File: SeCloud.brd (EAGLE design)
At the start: 107.2 x 69.7 mm, 94 parts, among them Q1 E4SB25.000F20E15(25MHz/20pF/2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, U3 SY6280, U7 MP1482DS, U8 RTL8211CL-GR

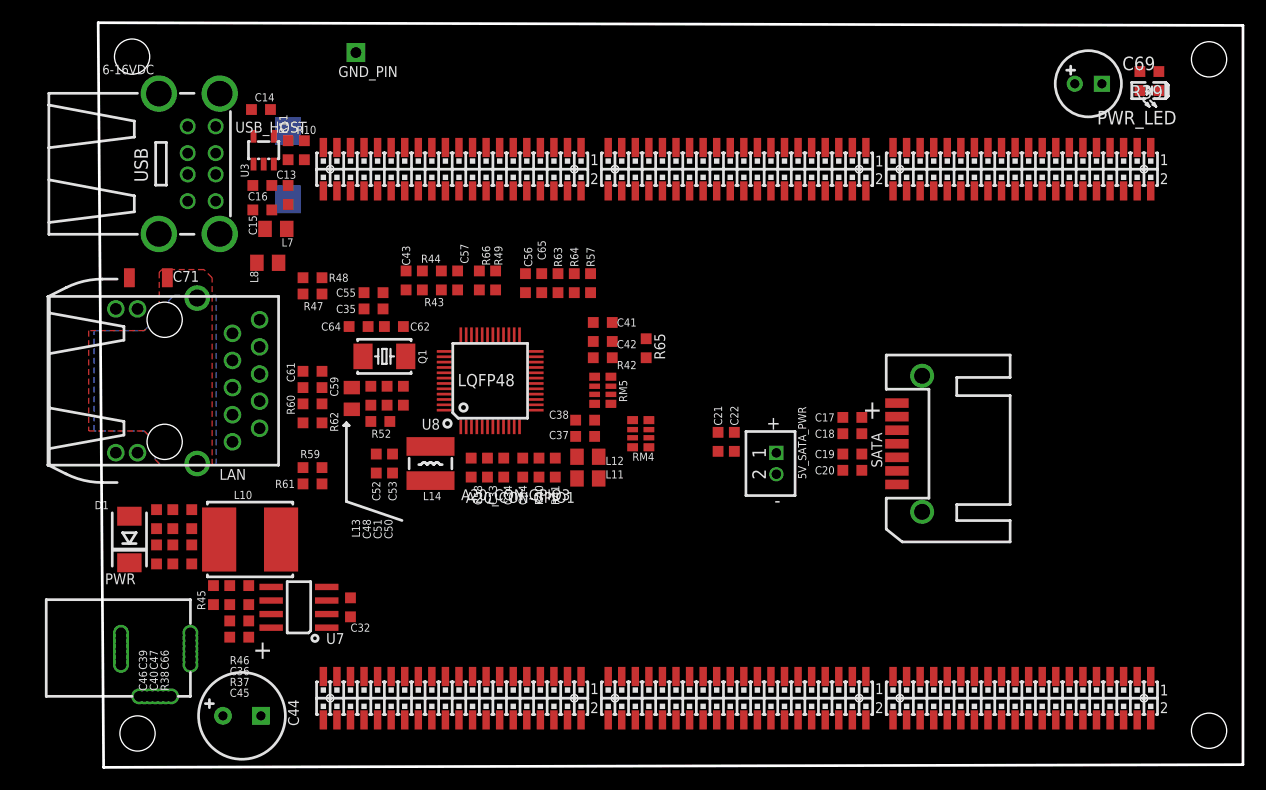
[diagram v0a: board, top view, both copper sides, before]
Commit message: Added lbr, RTL8188 module, and SATA connector;
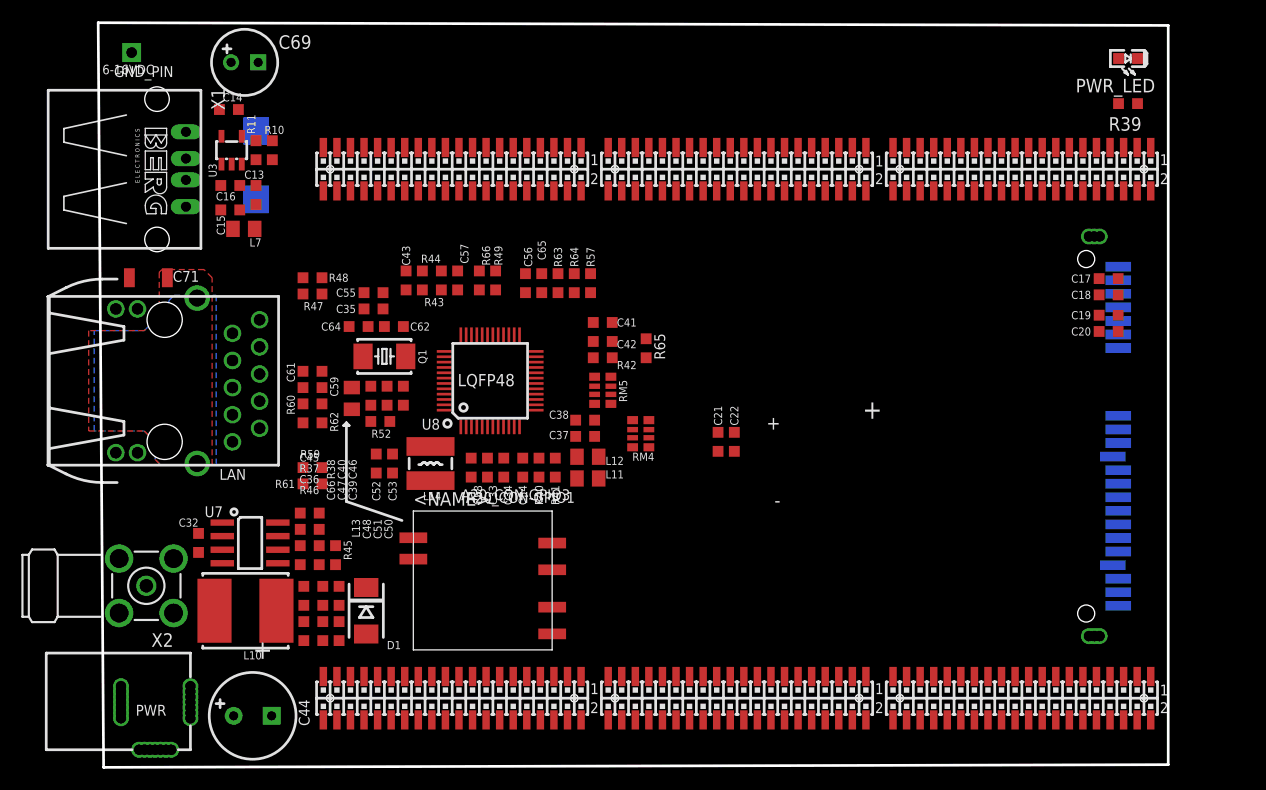
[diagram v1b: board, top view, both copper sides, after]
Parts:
- removed 5V_SATA_PWR: DW02S, Penko:DW02S
- removed L8: FB0805/600R/2A, rcl:L0805_5MIL_DWS
- removed SATA: SATA-PWA-07, OLIMEX_CONNECTORS:SATA-PWA-07
- removed USB_HOST: USB_TWO_LEVEL, OLIMEX_CONNECTORS:USB_TWO_LEVEL
- added U$1: RTL8188CUS-MOD, SeCloud:RTL8188CUS-MOD
- added U$2: SATA-CON, SeCloud:SATA-CON
- added X1: (no value), con-berg:PN87520
- added X2: BU-SMA-H, con-coax:BU-SMA-H
- moved C69 79.0 mm to (13.2, 66.0)
- moved C17 27.3 mm to (94.1, 45.8)
- moved C18 27.3 mm to (94.1, 44.2)
- moved C19 27.3 mm to (94.1, 42.3)
- moved C20 27.3 mm to (94.1, 40.8)
- moved D1 23.2 mm to (24.6, 14.7), turned to 270 degrees
- moved GND_PIN 21.0 mm to (2.62, 66.9)
- moved C39 20.1 mm to (22.0, 12.8), turned to 270 degrees
- moved C46 17.5 mm to (22.0, 16.1), turned to 90 degrees
- moved C47 17.5 mm to (20.5, 12.8), turned to 270 degrees
- moved C32 15.5 mm to (8.89, 21.0), turned to 270 degrees
- moved C66 14.8 mm to (18.7, 12.8), turned to 270 degrees
- moved C40 14.6 mm to (20.5, 16.1), turned to 90 degrees
- moved C45 13.4 mm to (19.3, 23.8), turned to 0 degrees
- moved R45 12.0 mm to (21.7, 19.9), turned to 270 degrees
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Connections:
- removed net N$193: L8.2, USB_HOST.GND1, USB_HOST.GND2, USB_HOST.GND3, USB_HOST.GND4
- new net ANT: U$1.ANT, X2.1
- net +5V: now also U$2.P7, U$2.P8, U$2.P9; no longer 5V_SATA_PWR.1
- net GND: now also U$1.GND, U$1.RF_GND, U$2.D1, U$2.D4, U$2.D7, U$2.P10, U$2.P12, U$2.P4, U$2.P5, U$2.P6, X1.4, X2.2, X2.3, X2.4, X2.5; no longer 5V_SATA_PWR.2, L8.1, SATA.1, SATA.4, SATA.7, USB_HOST.2.4
- net N$106: now also U$2.D2; no longer SATA.2
- net N$112: now also U$2.D3; no longer SATA.3
- net N$113: now also U$2.D5; no longer SATA.5
- net N$114: now also U$2.D6; no longer SATA.6
- net N$194: now also X1.1; no longer USB_HOST.2.1
- net UDM1: now also U$1.D-
- net UDM2: now also X1.2; no longer USB_HOST.2.2
- net UDP1: now also U$1.D+
- net UDP2: now also X1.3; no longer USB_HOST.2.3
- net VCC: now also U$1.3V3
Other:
- board size 107.2 x 69.7 mm -> 100.2 x 69.7 mm
